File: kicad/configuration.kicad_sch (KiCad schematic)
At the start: 29 parts, among them U1 MIMXRT1171DVMAB, U6 W25Q64JWUUIQ, U7 MKL26Z128VFM4, Y2 16MHz

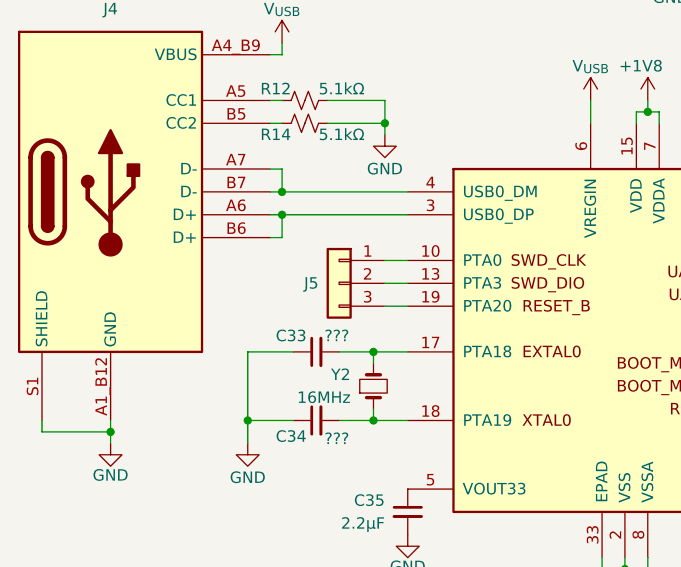
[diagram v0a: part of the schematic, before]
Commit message: added RTC battery connector
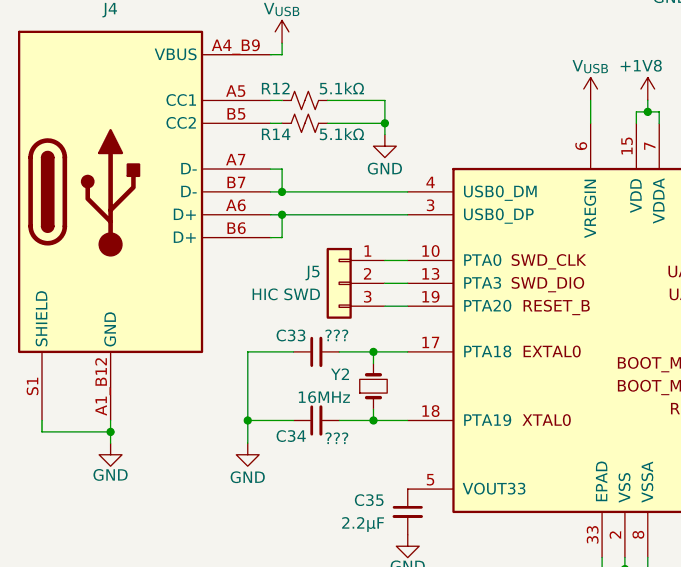
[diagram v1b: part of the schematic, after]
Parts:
- J4: value (none) -> USB C
- J5: value (none) -> HIC SWD
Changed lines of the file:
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@@
 		(dnp no)
 		(property "Reference" "J5"
-			(at 90.424 123.19 0)
+			(at 90.678 121.92 0)
 			(show_name no)
 			(do_not_autoplace no)
@@
 			)
 		)
-		(property "Value" ""
-			(at 90.17 124.46 0)
-			(hide yes)
+		(property "Value" "HIC SWD"
+			(at 90.678 124.46 0)
 			(show_name no)
 			(do_not_autoplace no)
@@
 			)
 		)
-		(property "Value" ""
+		(property "Value" "USB C"
 			(at 57.15 95.25 0)
-			(show_name no)
-			(do_not_autoplace no)
+			(hide yes)
+			(show_name no)
+			(do_not_autoplace no)

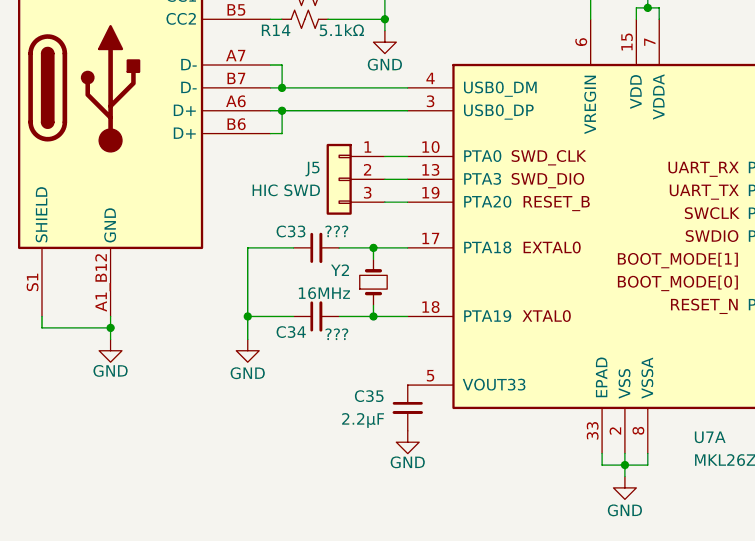
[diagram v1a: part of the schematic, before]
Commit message: added crystal footprints
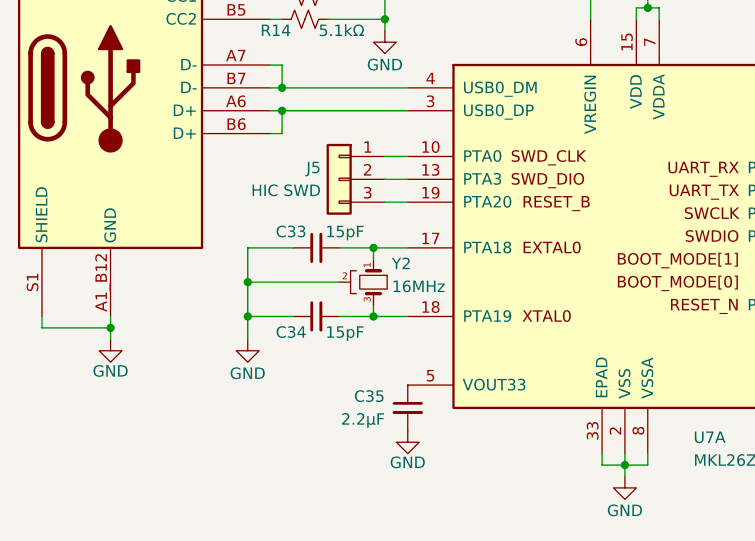
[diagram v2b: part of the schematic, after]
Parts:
- removed Y2: 16MHz, symbol Device:Crystal_Small
- added Y2: 16MHz, project_footprints:Crystal-4-Pin, symbol project_symbols:Crystal_GND24_Small
- C33, C34: value ??? -> 15pF; footprint (none) -> Capacitor_SMD:C_0402_1005Metric
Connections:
- net GND: now also Y2.2 (GND), Y2.4 (GND)
- net at C34.2, U7.18 (PTA19): now also Y2.3
- net at C33.2, U7.17 (PTA18): now also Y2.1
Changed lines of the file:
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@@
 	)
 	(junction
+		(at 82.55 134.62)
+		(diameter 0)
+		(color 0 0 0 0)
+	)
+	(junction
 		(at 303.53 101.6)
 		(diameter 0)
@@
 	(wire
 		(pts
+			(xy 82.55 134.62) (xy 82.55 138.43)
+		)
+		(stroke
+			(width 0)
+			(type default)
+		)
+	)
+	(wire
+		(pts
 			(xy 148.59 137.16) (xy 203.2 137.16)
 		)
@@
 	(wire
 		(pts
-			(xy 82.55 130.81) (xy 82.55 138.43)
+			(xy 82.55 130.81) (xy 82.55 134.62)
 		)
 		(stroke
@@
 	(wire
 		(pts
+			(xy 82.55 134.62) (xy 92.71 134.62)
+		)
+		(stroke
+			(width 0)
+			(type default)
+		)
+	)
+	(wire
+		(pts
 			(xy 303.53 116.84) (xy 303.53 119.38)
 		)
@@
 	)
 	(symbol
-		(lib_id "Device:R_Small_US")
-		(at 151.13 140.97 180)
+		(lib_id "project_symbols:Crystal_GND24_Small")
+		(at 96.52 134.62 270)
 		(unit 1)
 		(body_style 1)
@@
 		(in_pos_files yes)
 		(dnp no)
-		(property "Reference" "R22"
-			(at 152.654 142.24 0)
+		(property "Reference" "Y2"
+			(at 98.552 132.588 90)
 			(show_name no)
 			(do_not_autoplace no)
@@
 					(size 1.27 1.27)
 				)
-				(justify right)
+				(justify left)
 			)
 		)
-		(property "Value" "10kΩ"
-			(at 152.654 139.7 0)
+		(property "Value" "16MHz"
+			(at 98.552 135.128 90)
 			(show_name no)
 			(do_not_autoplace no)
@@
 					(size 1.27 1.27)
 				)
-				(justify right)
+				(justify left)
 			)
 		)
-		(property "Footprint" "Resistor_SMD:R_0201_0603Metric"
-			(at 151.13 140.97 0)
+		(property "Footprint" "project_footprints:Crystal-4-Pin"
+			(at 96.52 134.62 0)
 			(hide yes)
 			(show_name no)
@@
 		)
 		(property "Datasheet" ""
-			(at 151.13 140.97 0)
+			(at 96.52 134.62 0)
 			(hide yes)
 			(show_name no)
@@
 			)
 		)
-		(property "Description" "Resistor, small US symbol"
-			(at 151.13 140.97 0)
+		(property "Description" ""
+			(at 96.52 134.62 0)
 			(hide yes)
 			(show_name no)
@@
 			)
 		)
+		(pin "4"
+		)
 		(pin "2"
 		)
+		(pin "3"
+		)
 		(pin "1"
 		)
@@
 			(project "DEV-G2-NANO"
 				(path "/b6656e4d-fdee-4b90-a905-7068c060191f/45e1da5b-d52f-4e94-b563-4995febadb51"
-					(reference "R22")
+					(reference "Y2")
 					(unit 1)
 				)
@@
 	)
 	(symbol
-		(lib_id "power:GND")
-		(at 124.46 156.21 0)
+		(lib_id "Device:R_Small_US")
+		(at 151.13 140.97 180)
 		(unit 1)
 		(body_style 1)
@@
 		(in_pos_files yes)
 		(dnp no)
-		(property "Reference" "#PWR057"
-			(at 124.46 162.56 0)
-			(hide yes)
+		(property "Reference" "R22"
+			(at 152.654 142.24 0)
 			(show_name no)
 			(do_not_autoplace no)
@@
 					(size 1.27 1.27)
 				)
+				(justify right)
 			)
 		)
-		(property "Value" "GND"
-			(at 124.46 160.02 0)
+		(property "Value" "10kΩ"
+			(at 152.654 139.7 0)
 			(show_name no)
 			(do_not_autoplace no)
@@
 					(size 1.27 1.27)
 				)
+				(justify right)
 			)
 		)
-		(property "Footprint" ""
-			(at 124.46 156.21 0)
+		(property "Footprint" "Resistor_SMD:R_0201_0603Metric"
+			(at 151.13 140.97 0)
 			(hide yes)
 			(show_name no)
@@
 		)
 		(property "Datasheet" ""
-			(at 124.46 156.21 0)
+			(at 151.13 140.97 0)
 			(hide yes)
 			(show_name no)
@@
 			)
 		)
-		(property "Description" "Power symbol creates a global label with name \"GND\" , ground"
-			(at 124.46 156.21 0)
+		(property "Description" "Resistor, small US symbol"
+			(at 151.13 140.97 0)
 			(hide yes)
 			(show_name no)
@@
 			)
 		)
+		(pin "2"
+		)
 		(pin "1"
 		)
@@
 			(project "DEV-G2-NANO"
 				(path "/b6656e4d-fdee-4b90-a905-7068c060191f/45e1da5b-d52f-4e94-b563-4995febadb51"
-					(reference "#PWR057")
+					(reference "R22")
 					(unit 1)
 				)
@@
 	)
 	(symbol
-		(lib_id "Device:C_Small")
-		(at 90.17 138.43 90)
+		(lib_id "power:GND")
+		(at 124.46 156.21 0)
 		(unit 1)
 		(body_style 1)
@@
 		(in_pos_files yes)
 		(dnp no)
-		(property "Reference" "C34"
-			(at 87.376 140.208 90)
+		(property "Reference" "#PWR057"
+			(at 124.46 162.56 0)
+			(hide yes)
 			(show_name no)
 			(do_not_autoplace no)
@@
 			)
 		)
-		(property "Value" "???"
-			(at 92.456 140.462 90)
+		(property "Value" "GND"
+			(at 124.46 160.02 0)
 			(show_name no)
 			(do_not_autoplace no)
@@
 		)
 		(property "Footprint" ""
-			(at 90.17 138.43 0)
+			(at 124.46 156.21 0)
 			(hide yes)
 			(show_name no)
@@
 		)
 		(property "Datasheet" ""
-			(at 90.17 138.43 0)
+			(at 124.46 156.21 0)
 			(hide yes)
 			(show_name no)
@@
 			)
 		)
-		(property "Description" "Unpolarized capacitor, small symbol"
-			(at 90.17 138.43 0)
+		(property "Description" "Power symbol creates a global label with name \"GND\" , ground"
+			(at 124.46 156.21 0)
 			(hide yes)
 			(show_name no)
@@
 			)
 		)
-		(pin "2"
-		)
 		(pin "1"
 		)
@@
 			(project "DEV-G2-NANO"
 				(path "/b6656e4d-fdee-4b90-a905-7068c060191f/45e1da5b-d52f-4e94-b563-4995febadb51"
-					(reference "C34")
+					(reference "#PWR057")
 					(unit 1)
 				)
@@
 	)
 	(symbol
-		(lib_id "Device:Crystal_Small")
-		(at 96.52 134.62 270)
-		(mirror x)
-		(unit 1)
-		(body_style 1)
-		(exclude_from_sim no)
-		(in_bom yes)
-		(on_board yes)
-		(in_pos_files yes)
-		(dnp no)
-		(property "Reference" "Y2"
-			(at 93.98 133.3499 90)
-			(show_name no)
-			(do_not_autoplace no)
-			(effects
-				(font
-					(size 1.27 1.27)
-				)
-				(justify right)
-			)
-		)
-		(property "Value" "16MHz"
-			(at 93.98 135.8899 90)
-			(show_name no)
-			(do_not_autoplace no)
-			(effects
-				(font
-					(size 1.27 1.27)
-				)
-				(justify right)
-			)
-		)
-		(property "Footprint" ""
-			(at 96.52 134.62 0)
-			(hide yes)
-			(show_name no)
-			(do_not_autoplace no)
-			(effects
-				(font
-					(size 1.27 1.27)
-				)
-			)
-		)
-		(property "Datasheet" ""
-			(at 96.52 134.62 0)
-			(hide yes)
-			(show_name no)
-			(do_not_autoplace no)
-			(effects
-				(font
-					(size 1.27 1.27)
-				)
-			)
-		)
-		(property "Description" "Two pin crystal, small symbol"
-			(at 96.52 134.62 0)
-			(hide yes)
-			(show_name no)
-			(do_not_autoplace no)
-			(effects
-				(font
-					(size 1.27 1.27)
-				)
-			)
-		)
-		(pin "1"
-		)
-		(pin "2"
-		)
-		(instances
-			(project "DEV-G2-NANO"
-				(path "/b6656e4d-fdee-4b90-a905-7068c060191f/45e1da5b-d52f-4e94-b563-4995febadb51"
-					(reference "Y2")
-					(unit 1)
-				)
-			)
-		)
-	)
-	(symbol
 		(lib_id "power:+1V0")
 		(at 184.15 83.82 0)
@@
 			)
 		)
-		(property "Value" "???"
-			(at 92.456 129.032 90)
+		(property "Value" "15pF"
+			(at 91.186 129.032 90)
 			(show_name no)
 			(do_not_autoplace no)
@@
 					(size 1.27 1.27)
 				)
+				(justify right)
 			)
 		)
-		(property "Footprint" ""
+		(property "Footprint" "Capacitor_SMD:C_0402_1005Metric"
 			(at 90.17 130.81 0)
 			(hide yes)
@@
 					(unit 1)
 				)
+			)
+		)
+	)
+	(symbol
+		(lib_id "Device:C_Small")
+		(at 90.17 138.43 90)
+		(mirror x)
+		(unit 1)
+		(body_style 1)
+		(exclude_from_sim no)
+		(in_bom yes)
+		(on_board yes)
+		(in_pos_files yes)
+		(dnp no)
+		(property "Reference" "C34"
+			(at 87.376 140.208 90)
+			(show_name no)
+			(do_not_autoplace no)
+			(effects
+				(font
+					(size 1.27 1.27)
+				)
+			)
+		)
+		(property "Value" "15pF"
+			(at 91.186 140.208 90)
+			(show_name no)
+			(do_not_autoplace no)
+			(effects
+				(font
+					(size 1.27 1.27)
+				)
+				(justify right)
+			)
+		)
+		(property "Footprint" "Capacitor_SMD:C_0402_1005Metric"
+			(at 90.17 138.43 0)
+			(hide yes)
+			(show_name no)
+			(do_not_autoplace no)
+			(effects
+				(font
+					(size 1.27 1.27)
+				)
+			)
+		)
+		(property "Datasheet" ""
+			(at 90.17 138.43 0)
+			(hide yes)
+			(show_name no)
+			(do_not_autoplace no)
+			(effects
+				(font
+					(size 1.27 1.27)
+				)
+			)
+		)
+		(property "Description" "Unpolarized capacitor, small symbol"
+			(at 90.17 138.43 0)
+			(hide yes)
+			(show_name no)
+			(do_not_autoplace no)
+			(effects
+				(font
+					(size 1.27 1.27)
+				)
+			)
+		)
+		(pin "2"
+		)
+		(pin "1"
+		)
+		(instances
+			(project "DEV-G2-NANO"
+				(path "/b6656e4d-fdee-4b90-a905-7068c060191f/45e1da5b-d52f-4e94-b563-4995febadb51"
+					(reference "C34")
+					(unit 1)
+				)

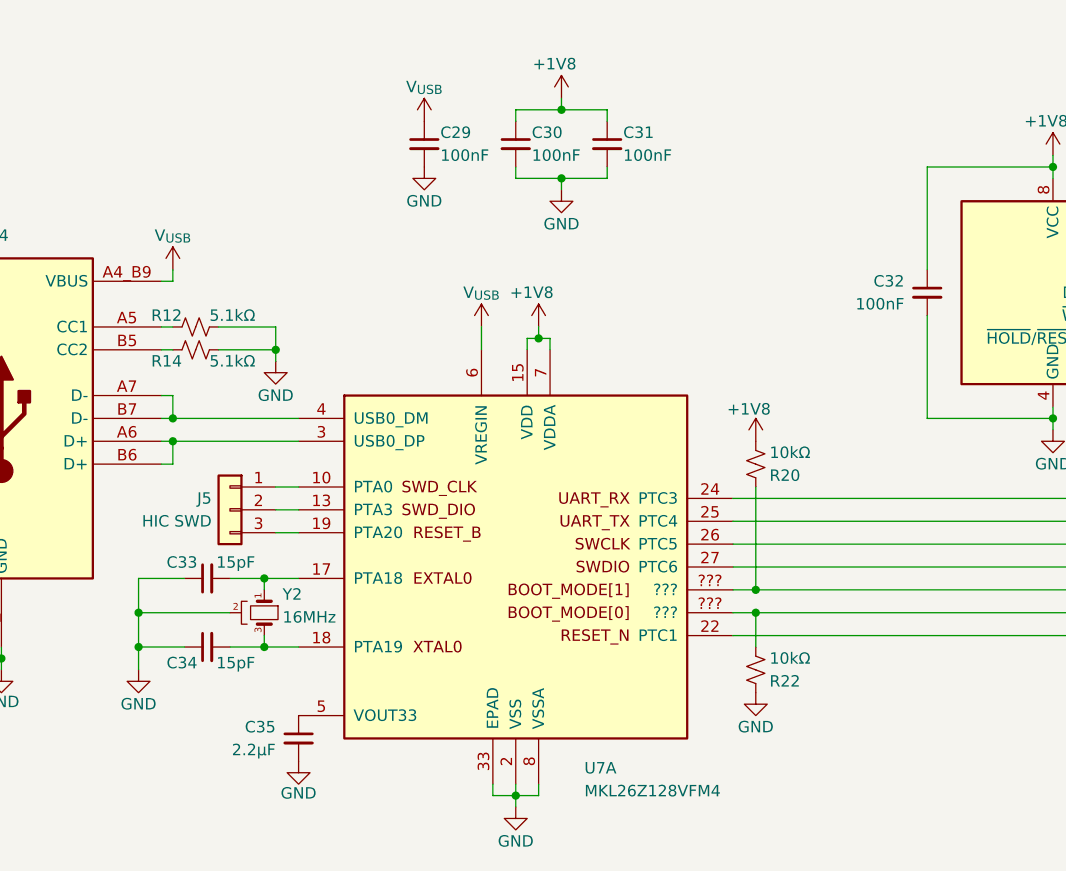
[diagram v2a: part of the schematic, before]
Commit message: reworked bypass capacitors for MIMXRT1171DVMAB
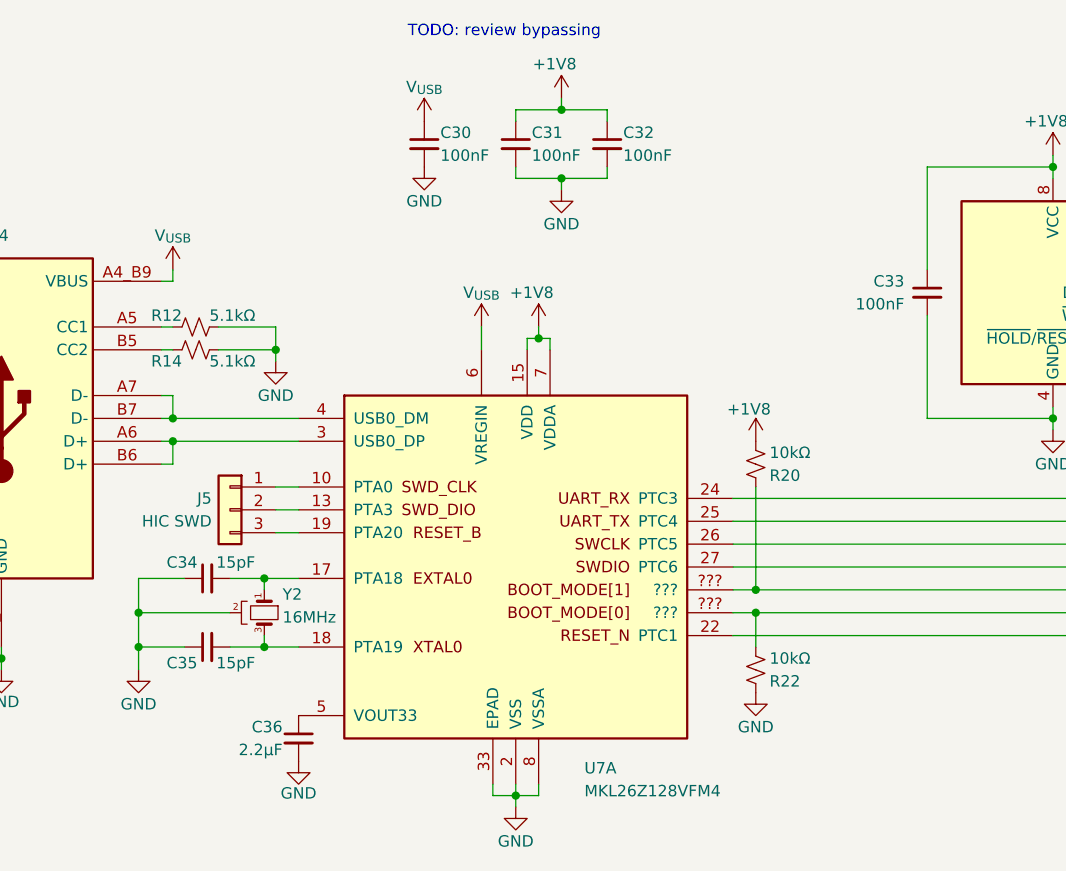
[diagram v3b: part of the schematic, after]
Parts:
- removed C35: 2.2µF, symbol Device:C_Small
- added C36: 2.2μF, symbol Device:C_Small
- renumbered C29 to C30, C30 to C31, C31 to C32, C32 to C33, C33 to C34, C34 to C35
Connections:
- net GND: now also C36.2
- net at U7.5 (VOUT33): now also C36.1
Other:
- note added: "TODO: review bypassing"

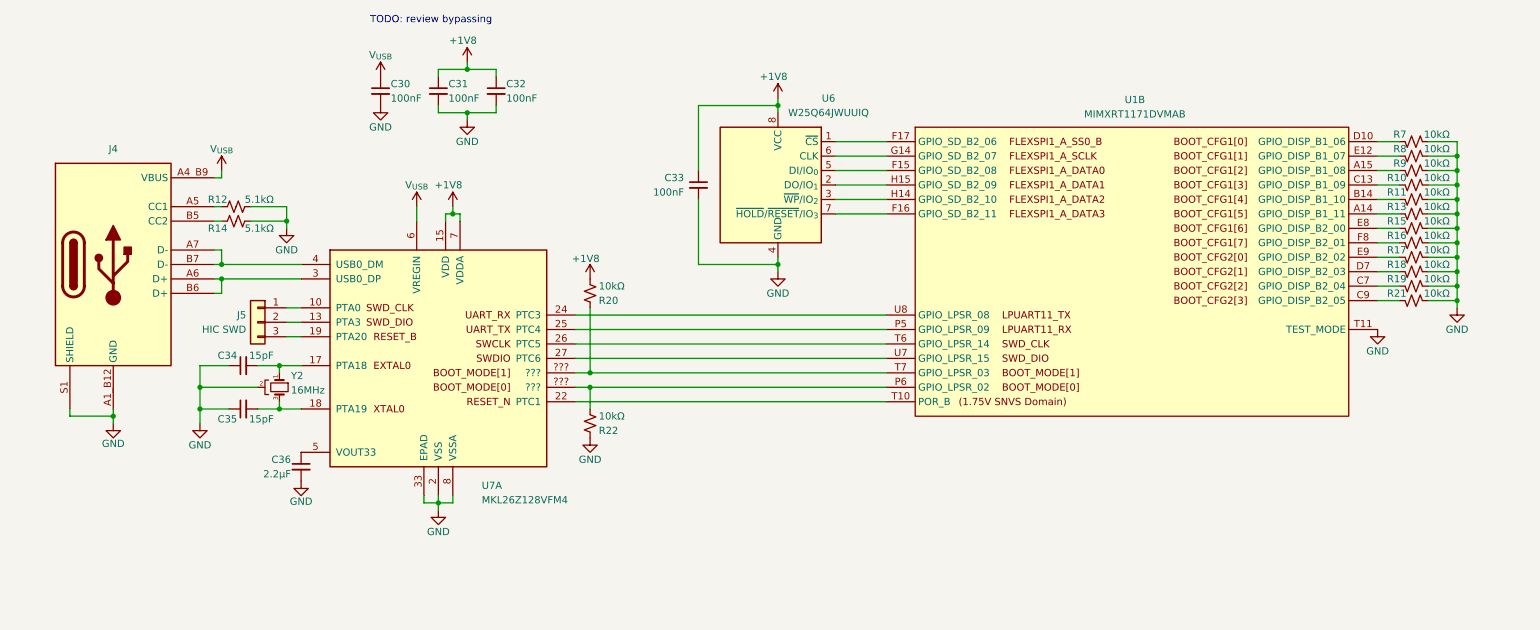
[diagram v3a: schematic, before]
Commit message: reworked USB circuitry
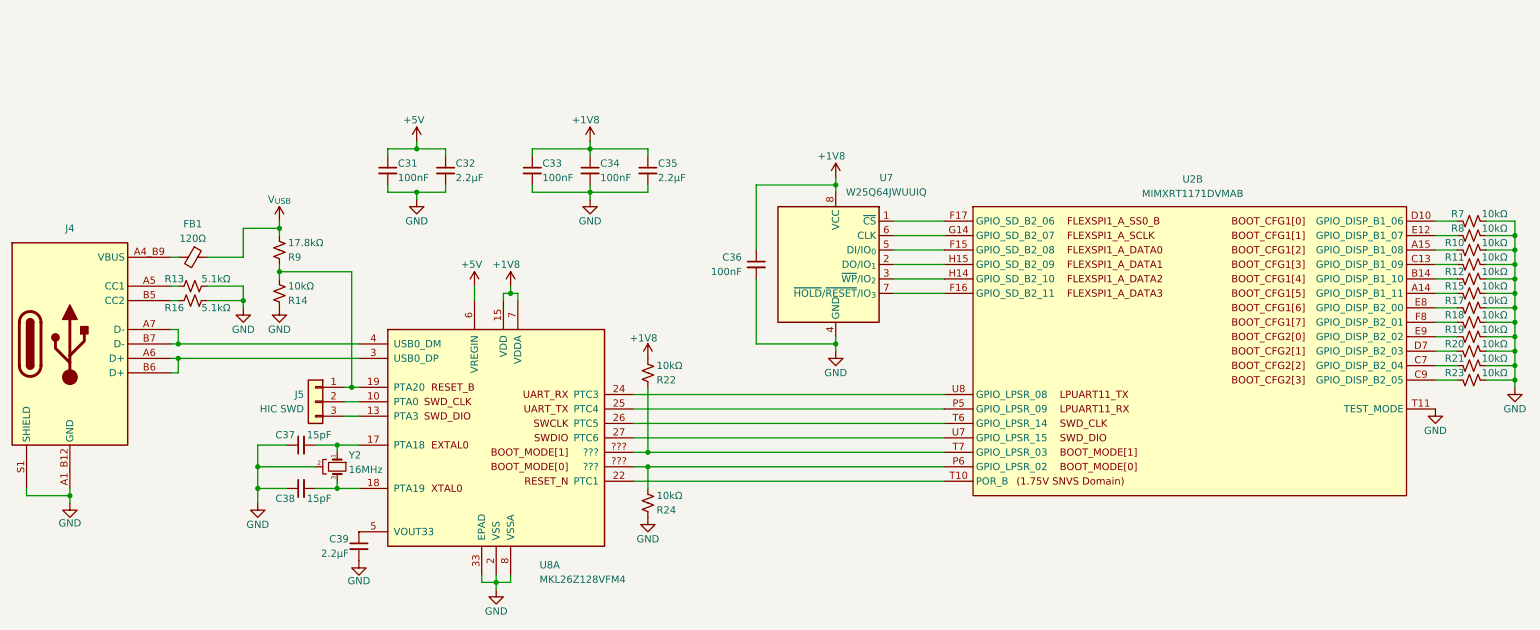
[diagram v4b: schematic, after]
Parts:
- added C32, C35: 2.2μF, Capacitor_SMD:C_0201_0603Metric, symbol Device:C_Small
- added FB1: 120Ω, symbol Device:FerriteBead_Small
- added R14: 10kΩ, Resistor_SMD:R_0201_0603Metric, symbol Device:R_Small_US
- added R9: 17.8kΩ, symbol Device:R_Small_US
- U8: renamed from U7; footprint project_footprints:MKL26Z128VFM4 -> Package_DFN_QFN:QFN-32-1EP_5x5mm_P0.5mm_EP3.45x3.45mm
- renumbered C30 to C31, C31 to C33, C32 to C34, C33 to C36, C34 to C37, C35 to C38, C36 to C39, R9 to R10, R10 to R11, R11 to R12, R12 to R13, R13 to R15, R14 to R16, R15 to R17, R16 to R18, R17 to R19, R18 to R20, R19 to R21, R20 to R22, R21 to R23, R22 to R24, U1 to U2, U6 to U7
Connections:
- net +1V8: now also C35.1
- net GND: now also C32.2, C35.2, R14.1
- net V_{USB}: now also FB1.1, R9.2; no longer C31.1, J4.A4_B9 (VBUS), J4.B4_A9 (VBUS), U8.6 (VREGIN)
- net at J5.1 (Pin_1): now also U8.19 (PTA20), R14.2, R9.1; no longer U8.10 (PTA0)
- net at J5.2 (Pin_2): now also U8.10 (PTA0); no longer U8.13 (PTA3)
- net at J5.3 (Pin_3): now also U8.13 (PTA3); no longer U8.19 (PTA20)
- new net: FB1.2, J4.A4_B9 (VBUS), J4.B4_A9 (VBUS)
- new net +5V: C31.1, C32.1, U8.6 (VREGIN)
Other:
- note removed: "TODO: review bypassing"
- moved on the sheet: C31, C33, C34, C36, C37, C38, C39, J4, J5, R10, R11, R12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
